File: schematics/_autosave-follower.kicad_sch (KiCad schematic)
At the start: 26 parts, among them M2 Motor, M3 Motor, Q1 TLE5206_2S, Q2 TLE5206_2S, SW5 Reset, U10 PIC32MX170F256B, U5 Tape_Left, U6 Tape_Middle, U7 Tape_Right, U8 Quadrature_Encoder, U9 Quadrature_Encoder

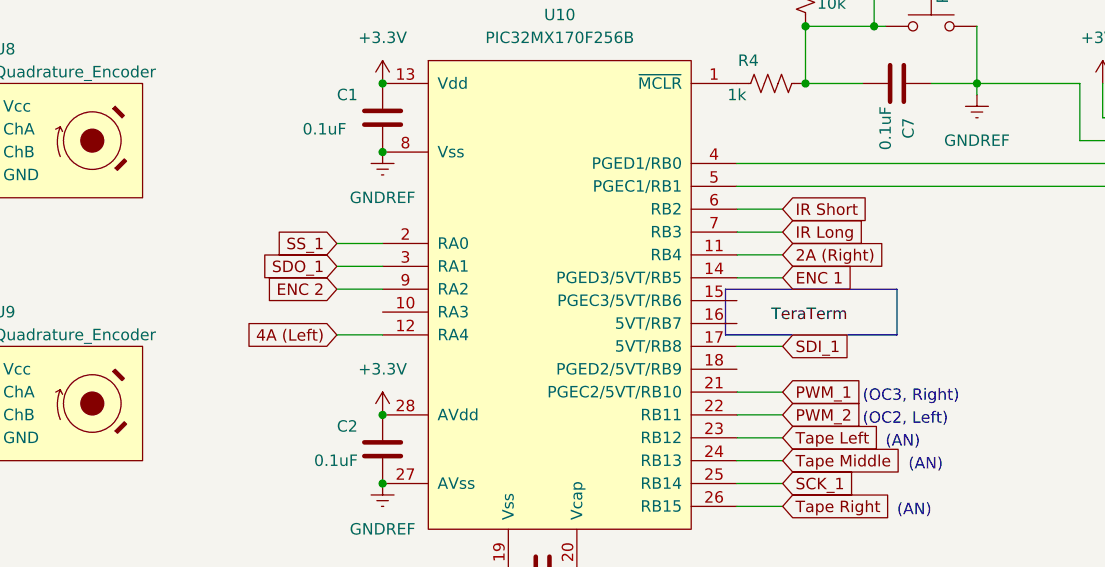
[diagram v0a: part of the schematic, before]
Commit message: Annotate left and right motor on pin leader PIC schematic.
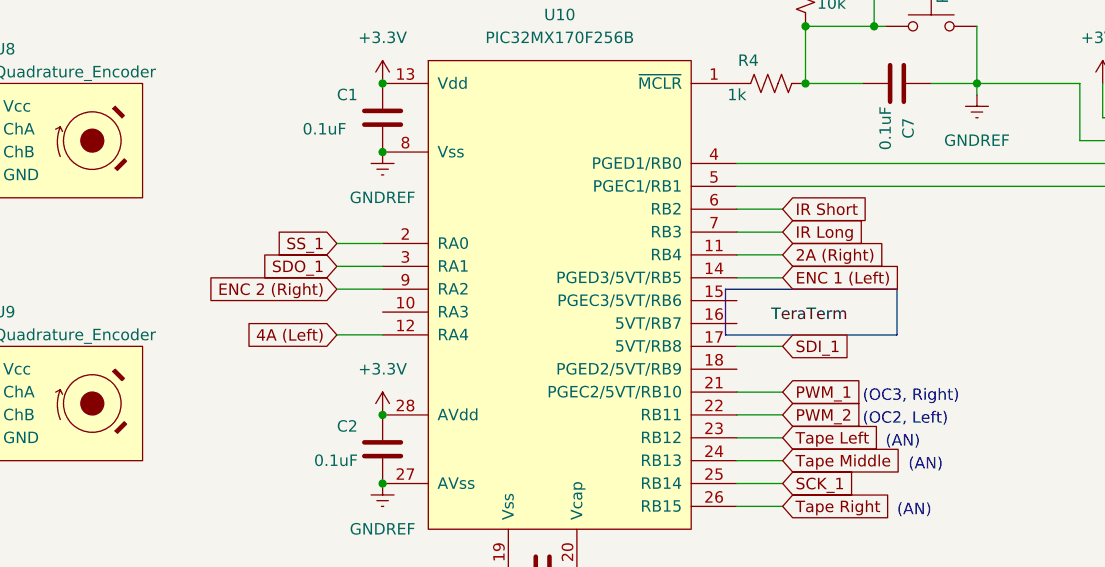
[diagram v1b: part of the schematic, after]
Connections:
- net ENC 1: no longer U10.14 (PGED3/5VT/RB5)
- net ENC 2: no longer U10.9 (RA2)
- new net ENC 1 (Left): U10.14 (PGED3/5VT/RB5)
- new net ENC 2 (Right): U10.9 (RA2)
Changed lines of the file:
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@@
     )
   )
-  (global_label "ENC 1" (shape input) (at 217.17 57.15 0) (fields_autoplaced)
+  (global_label "ENC 1 (Left)" (shape input) (at 217.17 57.15 0) (fields_autoplaced)
     (effects (font (size 1.27 1.27)) (justify left))
-    (property "Intersheet References" "${INTERSHEET_REFS}" (id 0) (at 225.5098 57.2294 0)
+    (property "Intersheet References" "${INTERSHEET_REFS}" (id 0) (at 231.7388 57.0706 0)
       (effects (font (size 1.27 1.27)) (justify left) hide)
     )
@@
     )
   )
-  (global_label "ENC 2" (shape input) (at 167.64 58.42 180) (fields_autoplaced)
+  (global_label "ENC 2 (Right)" (shape input) (at 167.64 58.42 180) (fields_autoplaced)
     (effects (font (size 1.27 1.27)) (justify right))
-    (property "Intersheet References" "${INTERSHEET_REFS}" (id 0) (at 159.3002 58.3406 0)
+    (property "Intersheet References" "${INTERSHEET_REFS}" (id 0) (at 151.7407 58.3406 0)
       (effects (font (size 1.27 1.27)) (justify right) hide)
     )
